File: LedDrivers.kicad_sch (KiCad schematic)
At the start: 40 parts, among them Q1 HL2309, Q2 HL2309, Q3 HL2309, Q4 HL2309, Q5 HL2309, U1 LTV-5314-TP1, U2 LTV-5314-TP1, U3 LTV-5314-TP1, U4 LTV-5314-TP1, U5 LTV-5314-TP1

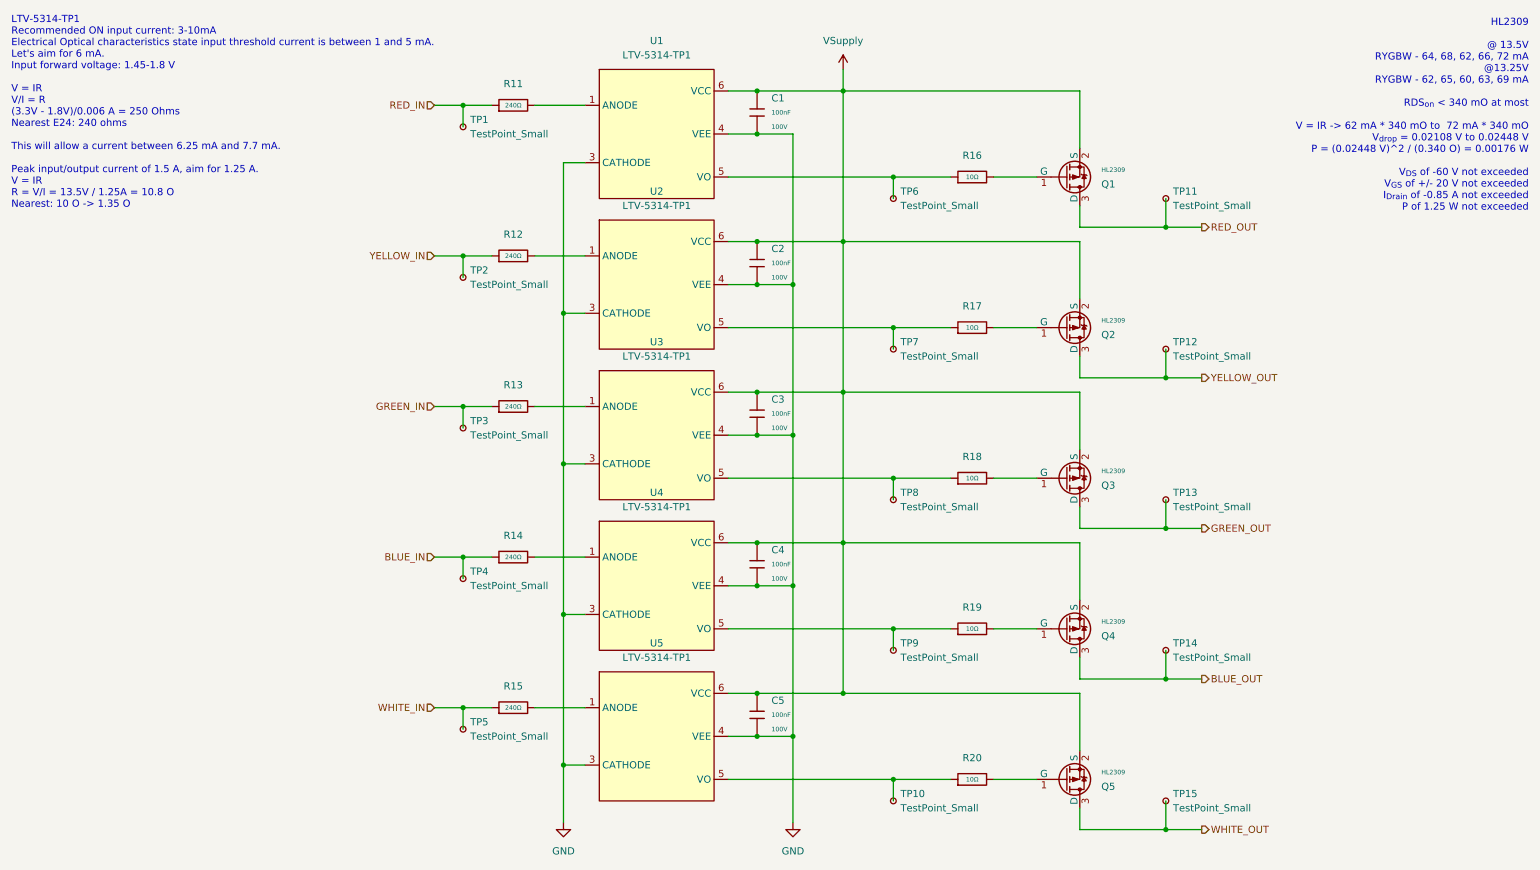
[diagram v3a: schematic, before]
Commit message: DRC adjustments
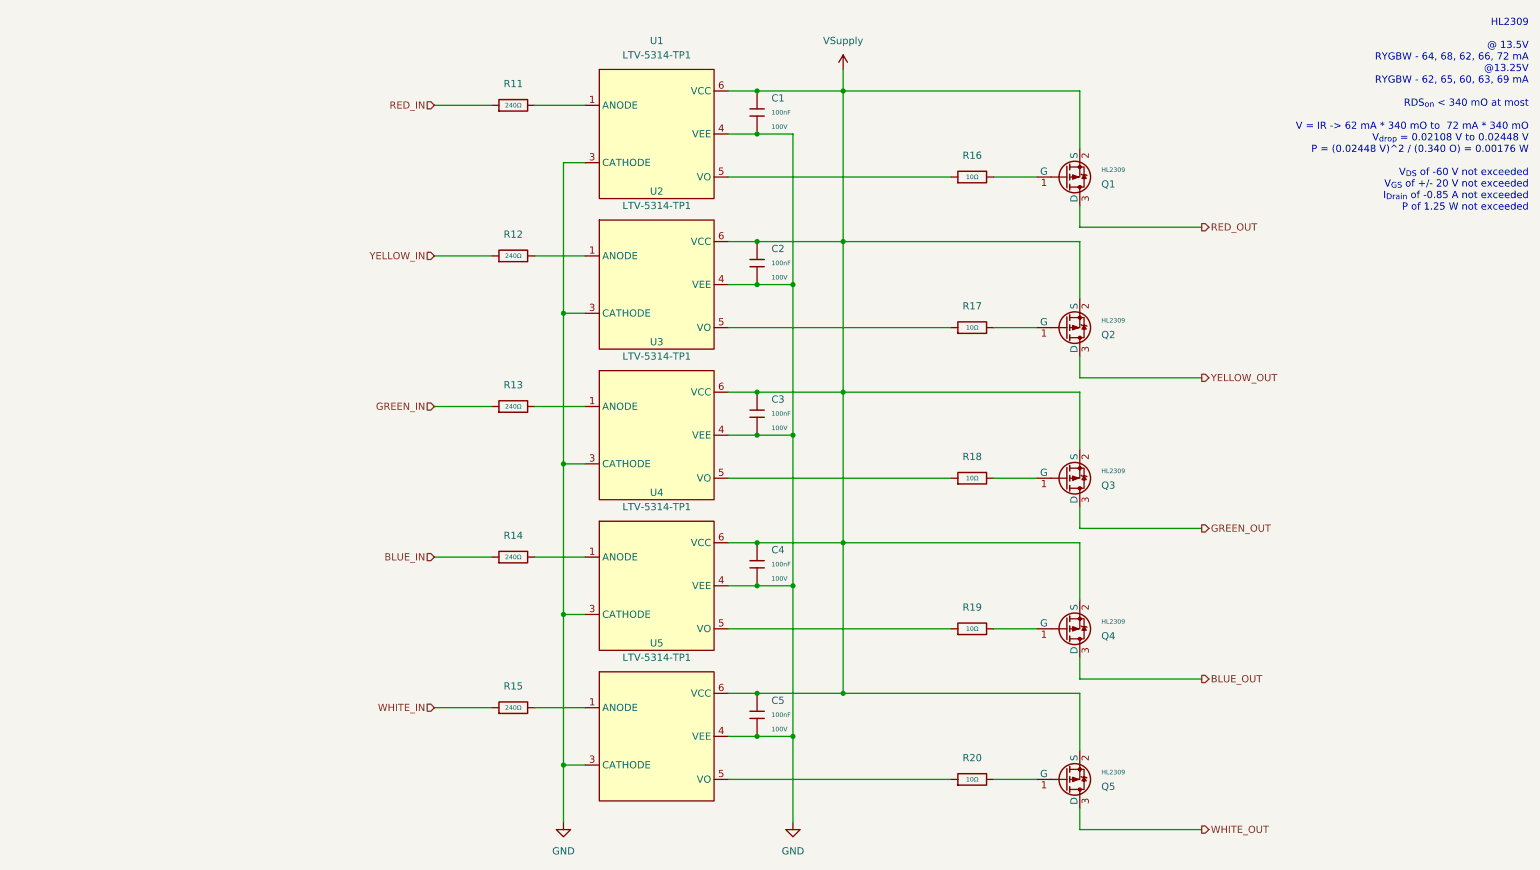
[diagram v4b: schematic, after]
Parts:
- removed TP1, TP10, TP11, TP12, TP13, TP14, TP15, TP2, TP3, TP4, TP5, TP6, TP7, TP8, TP9: TestPoint_Small, symbol Connector:TestPoint_Small
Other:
- note removed: "LTV-5314-TP1 Recommended ON input current: 3-10mA Electrical Optical characteristics state input threshold current is between 1 and 5 mA. Let's aim for 6 mA. Input forward voltage: 1.45-1.8 V V = IR V/I = R (3.3V - 1.8V)/0.006 A = 250 Ohms Nearest E24: 240 ohms This will allow a current between 6.25 mA and 7.7 mA. Peak input/output current of 1.5 A, aim for 1.25 A. V = IR R = V/I = 13.5V / 1.25A 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"
